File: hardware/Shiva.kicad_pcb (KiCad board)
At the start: 2 copper layers, 99.8 x 99.8 mm, 77 parts, among them J1 JACK_FEMALE_STEREO, J2 JACK_FEMALE_STEREO, J3 JACK_FEMALE_STEREO, J4 JACK_FEMALE_STEREO, J5 JACK_FEMALE_STEREO, J6 JACK_FEMALE_STEREO, J7 JACK_FEMALE_STEREO, J8 JACK_FEMALE_STEREO, P1 DIN_5, U1 LTC6242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

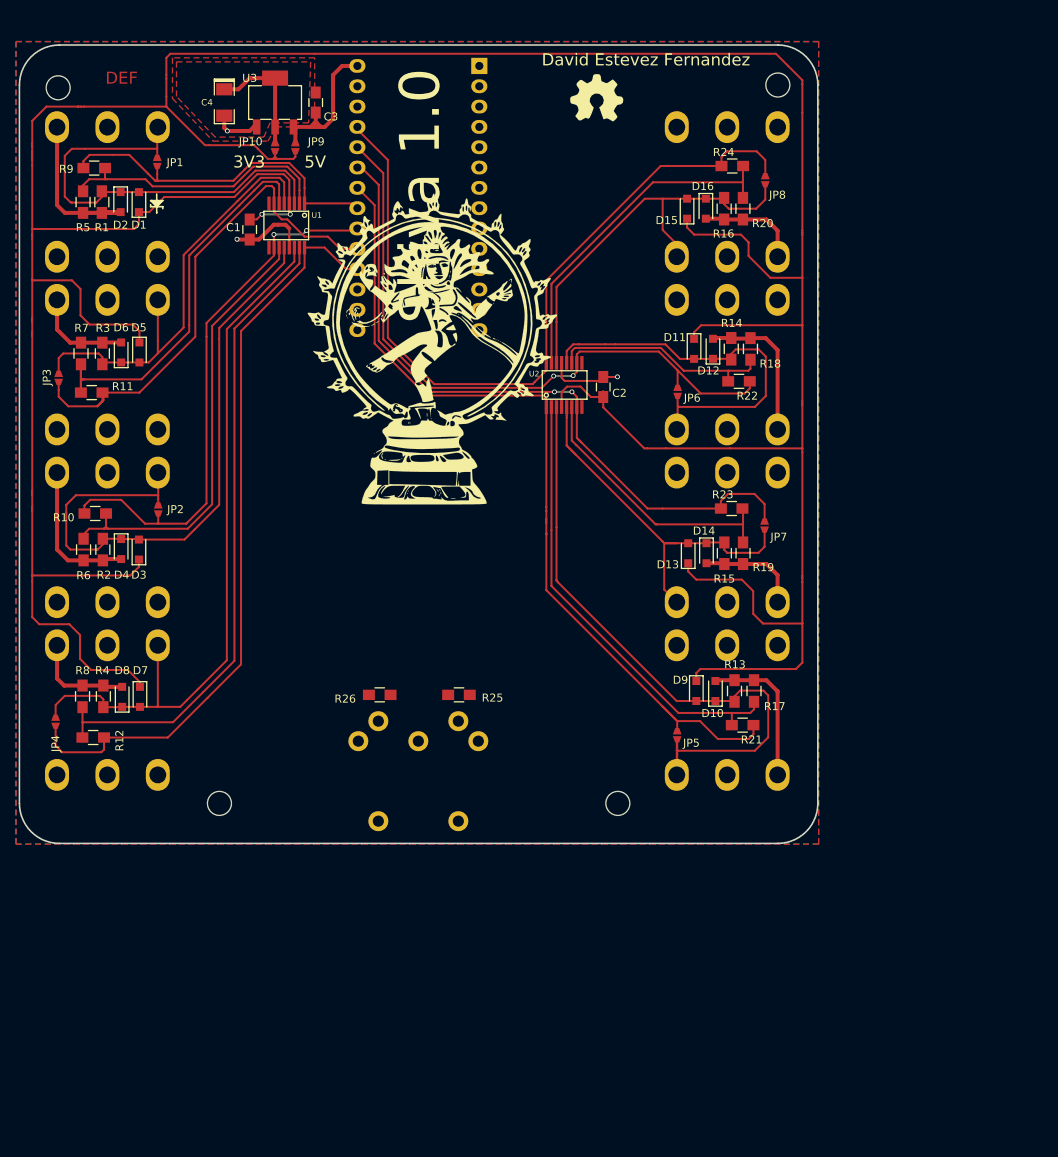
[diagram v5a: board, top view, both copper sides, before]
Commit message: Fill zones, connect remaining stuff, beautify tracks
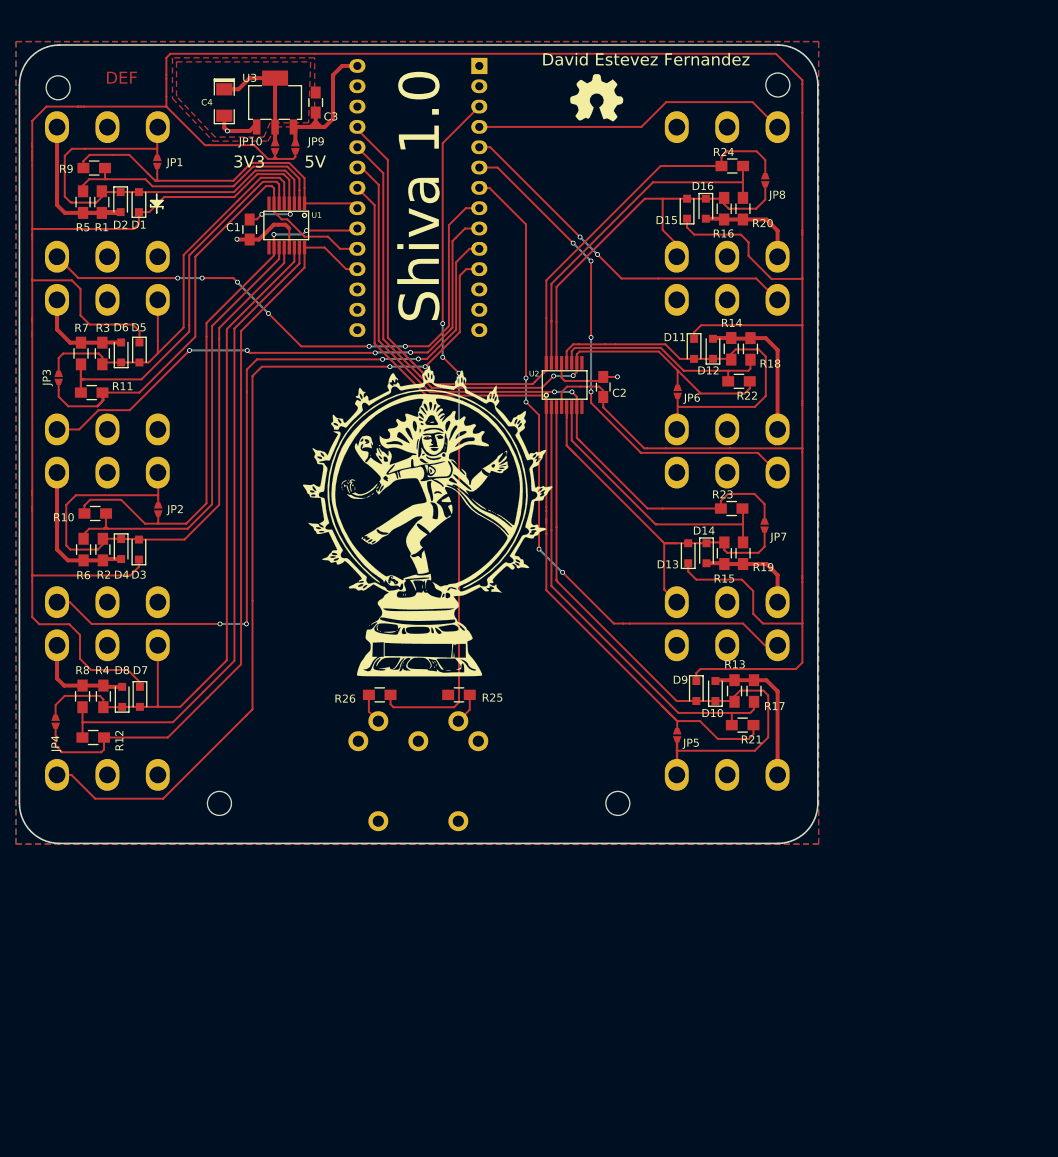
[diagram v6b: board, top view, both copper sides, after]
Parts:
- moved G*** 21.9 mm to (144.3, 106.9)
- moved G*** 21.5 mm to (145.3, 112.2)
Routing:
- net /DETECT_01: track 2.12 -> 112.1 mm, vias 0 -> 2
- net /DETECT_02: track 2.12 -> 99.0 mm, vias 0 -> 4
- net /TX: track 0.00 -> 87.4 mm, vias 0 -> 4
- net /DETECT_08: track 1.15 -> 84.9 mm, vias 0 -> 4
- net /DETECT_04: track 3.09 -> 75.1 mm, vias 0 -> 6
- net /DETECT_03: track 0.97 -> 70.8 mm, vias 0 -> 4
- net /DETECT_07: track 2.12 -> 65.6 mm, vias 0 -> 4
- net /DETECT_06: track 1.76 -> 46.9 mm, vias 0 -> 2
- net /DETECT_05: track 1.15 -> 41.0 mm
- net Net-(P1-Pad5): track 0.00 -> 3.88 mm
- net Net-(P1-Pad4): track 0.00 -> 3.78 mm

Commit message: Route LED for channel 1
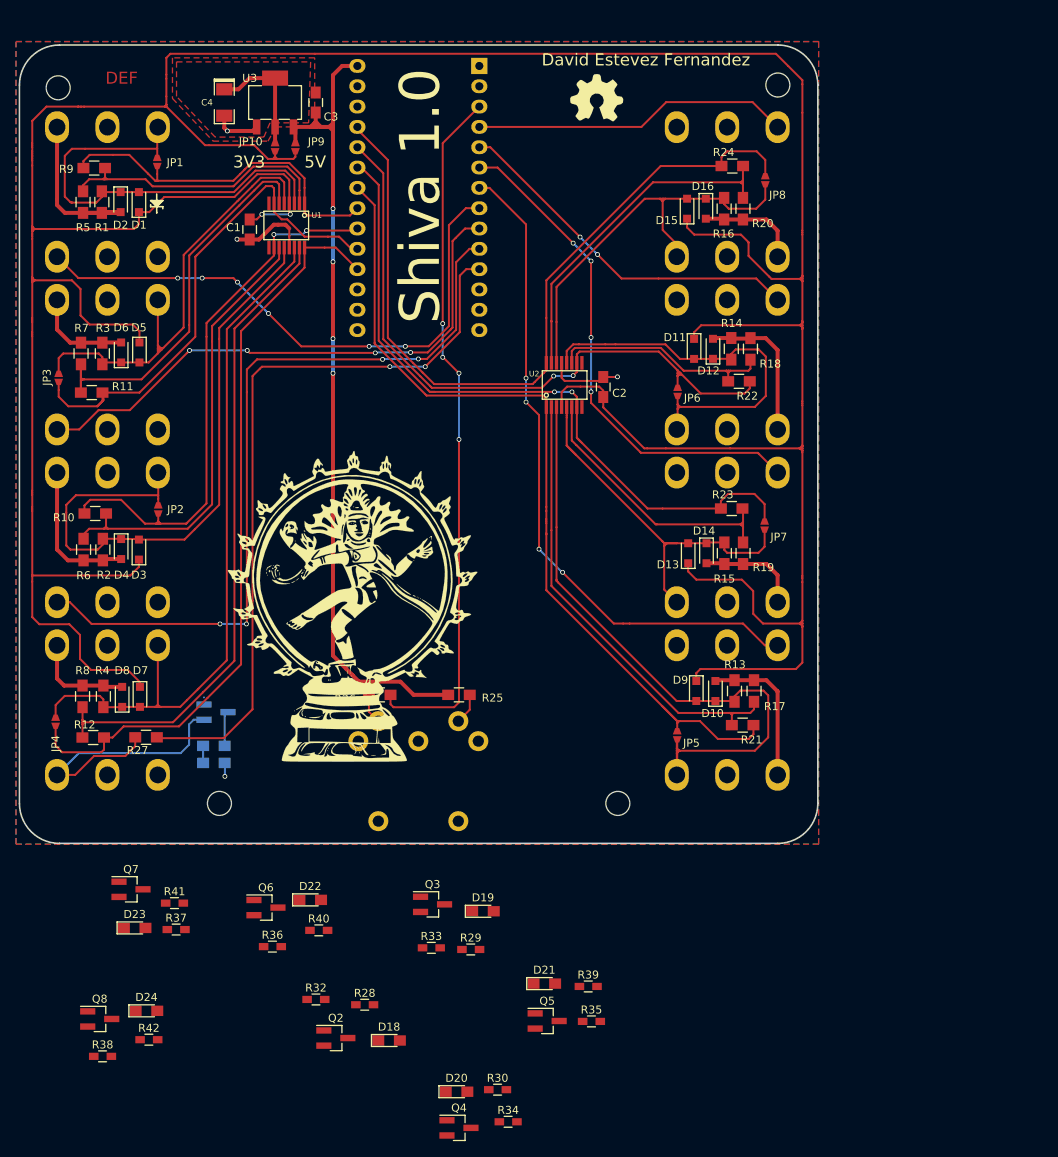
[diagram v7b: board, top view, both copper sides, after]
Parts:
- added D17: LED, LEDs:LED_0805_HandSoldering, B.Cu at (118.7, 142.5)
- added D18: LED, LEDs:LED_0805_HandSoldering, F.Cu at (140.6, 177.2)
- added D19: LED, LEDs:LED_0805_HandSoldering, F.Cu at (152.3, 161.0)
- added D20: LED, LEDs:LED_0805_HandSoldering, F.Cu at (149.0, 183.6)
- added D21: LED, LEDs:LED_0805_HandSoldering, F.Cu at (160.0, 170.1)
- added D22: LED, LEDs:LED_0805_HandSoldering, F.Cu at (130.8, 159.6)
- added D23: LED, LEDs:LED_0805_HandSoldering, F.Cu at (108.8, 163.1)
- added D24: LED, LEDs:LED_0805_HandSoldering, F.Cu at (110.3, 173.5)
- added Q1: 2N7002, TO_SOT_Packages_SMD:SOT-23_Handsoldering, B.Cu at (119.0, 136.1)
- added Q2: 2N7002, TO_SOT_Packages_SMD:SOT-23_Handsoldering, F.Cu at (134.0, 176.9)
- added Q3: 2N7002, TO_SOT_Packages_SMD:SOT-23_Handsoldering, F.Cu at (146.1, 160.2)
- added Q4: 2N7002, TO_SOT_Packages_SMD:SOT-23_Handsoldering, F.Cu at (149.4, 188.1)
- added Q5: 2N7002, TO_SOT_Packages_SMD:SOT-23_Handsoldering, F.Cu at (160.4, 174.8)
- added Q6: 2N7002, TO_SOT_Packages_SMD:SOT-23_Handsoldering, F.Cu at (125.2, 160.6)
- added Q7: 2N7002, TO_SOT_Packages_SMD:SOT-23_Handsoldering, F.Cu at (108.4, 158.3)
- added Q8: 2N7002, TO_SOT_Packages_SMD:SOT-23_Handsoldering, F.Cu at (104.4, 174.5)
- added R27: 4K7, Resistors_SMD:R_0805_HandSoldering, F.Cu at (110.2, 139.3)
- added R28: 4K7, Resistors_SMD:R_0603_HandSoldering, F.Cu at (137.6, 172.7)
- added R29: 4K7, Resistors_SMD:R_0603_HandSoldering, F.Cu at (150.8, 165.8)
- added R30: 4K7, Resistors_SMD:R_0603_HandSoldering, F.Cu at (154.2, 183.3)
- added R31: 100R, Resistors_SMD:R_0805_HandSoldering, B.Cu at (118.7, 140.4)
- added R32: 100R, Resistors_SMD:R_0603_HandSoldering, F.Cu at (131.5, 172.1)
- added R33: 100R, Resistors_SMD:R_0603_HandSoldering, F.Cu at (145.9, 165.6)
- added R34: 100R, Resistors_SMD:R_0603_HandSoldering, F.Cu at (155.5, 187.4)
- added R35: 4K7, Resistors_SMD:R_0603_HandSoldering, F.Cu at (165.9, 174.8)
- added R36: 4K7, Resistors_SMD:R_0603_HandSoldering, F.Cu at (126.0, 165.5)
- added R37: 4K7, Resistors_SMD:R_0603_HandSoldering, F.Cu at (114.0, 163.3)
- added R38: 4K7, Resistors_SMD:R_0603_HandSoldering, F.Cu at (104.8, 179.2)
- added R39: 100R, Resistors_SMD:R_0603_HandSoldering, F.Cu at (165.5, 170.4)
- added R40: 100R, Resistors_SMD:R_0603_HandSoldering, F.Cu at (131.8, 163.4)
- added R41: 100R, Resistors_SMD:R_0603_HandSoldering, F.Cu at (113.8, 160.0)
- added R42: 100R, Resistors_SMD:R_0603_HandSoldering, F.Cu at (110.6, 177.1)
- moved G*** 14.2 mm to (135.9, 122.8)
- moved G*** 0.52 mm to (143.9, 124.0)
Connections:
- J1 pad SS: /DETECT_04 -> /CHANNEL_04_SW
- J2 pad SS: /DETECT_02 -> /CHANNEL_02_SW
- J3 pad SS: /DETECT_03 -> /CHANNEL_03_SW
- J4 pad SS: /DETECT_01 -> /CHANNEL_01_SW
- J5 pad SS: /DETECT_05 -> /CHANNEL_05_SW
- J6 pad SS: /DETECT_06 -> /CHANNEL_06_SW
- J7 pad SS: /DETECT_07 -> /CHANNEL_07_SW
- J8 pad SS: /DETECT_08 -> /CHANNEL_08_SW
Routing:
- net +5V: track 20.6 -> 105.4 mm, vias 0 -> 4
- net /CHANNEL_01_SW: track 0.00 -> 37.1 mm
- net /DETECT_07: track 65.6 -> 35.2 mm, vias 4 -> 3
- net /CHANNEL_07_SW: track 0.00 -> 30.4 mm, vias 0 -> 1
- net /DETECT_03: track 70.8 -> 41.5 mm, vias 4 -> 2
- net /CHANNEL_03_SW: track 0.00 -> 29.3 mm, vias 0 -> 2
- net /DETECT_02: track 99.0 -> 75.4 mm, vias 4 -> 3
- net /CHANNEL_02_SW: track 0.00 -> 23.6 mm, vias 0 -> 1
- net /DETECT_01: track 112.1 -> 93.6 mm
- net VCC: track 465.7 -> 474.2 mm, vias 2 -> 3
- net /CHANNEL_04_SW: track 0.00 -> 6.86 mm
- net /DETECT_04: track 75.1 -> 68.2 mm
- net /DETECT_05: track 41.0 -> 35.4 mm
- net /CHANNEL_05_SW: track 0.00 -> 5.57 mm
- net /CHANNEL_06_SW: track 0.00 -> 5.53 mm
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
